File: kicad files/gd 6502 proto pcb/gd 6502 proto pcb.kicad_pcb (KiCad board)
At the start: 4 copper layers, 86.4 x 48.3 mm, 37 parts, among them J1 POWER, J10 NOR-Extra, J11 ADDR_BUS, J12 ROMEN, J2 ADDR_BUS, J3 Main Data, J4 Bus Signals, J5 Address, J6 Data, J7 ROMDIR_SEL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

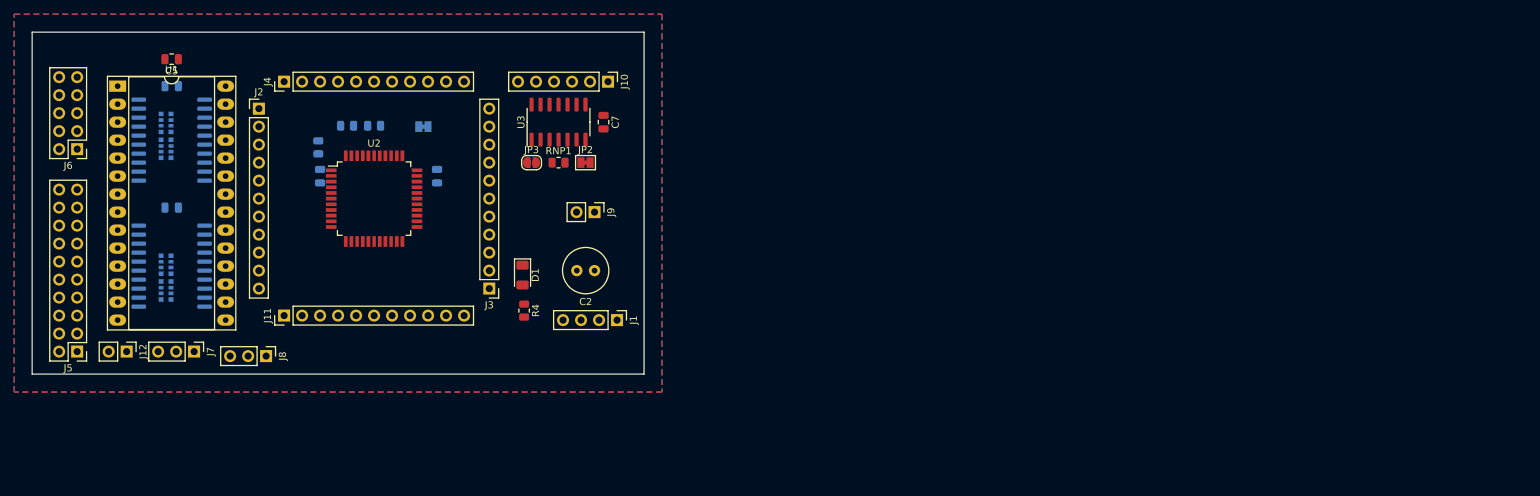
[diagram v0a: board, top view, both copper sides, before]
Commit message: can't put buffers under the eeprom. not enough room for all those address lines
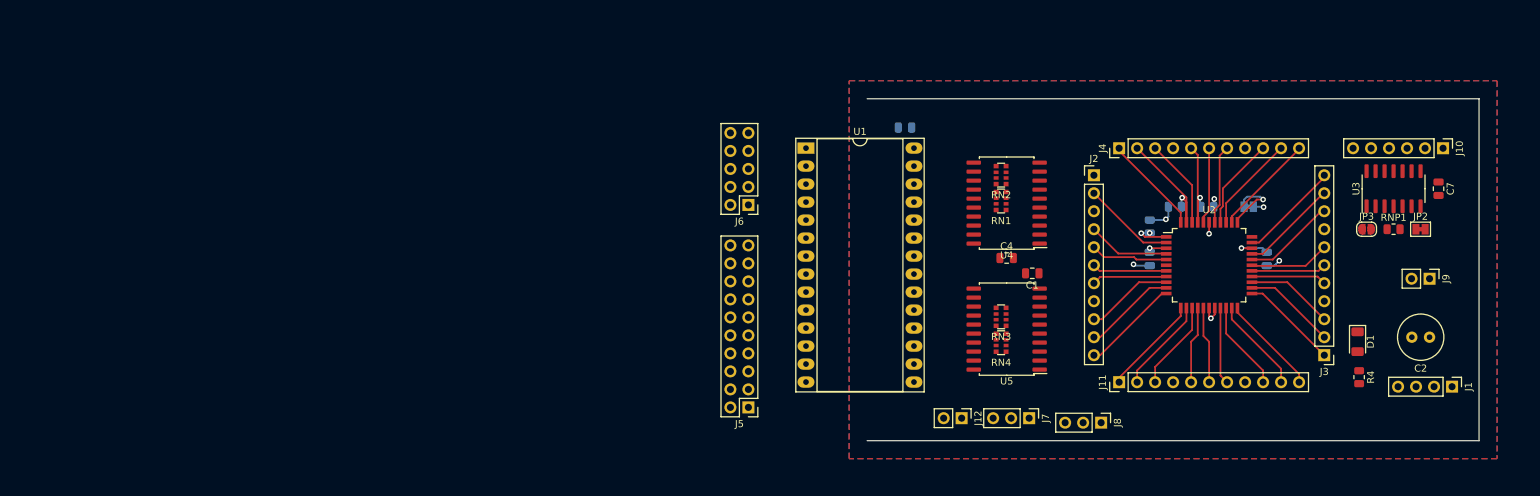
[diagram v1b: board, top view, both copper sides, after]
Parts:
- C1, C4, RN1, RN2, RN3, RN4, U4, U5: moved to F.Cu
- C5: moved to B.Cu
- moved C1 124.3 mm to (156.4, 89.9), turned to 180 degrees
- moved RN4 121.9 mm to (152.0, 99.7)
- moved U5 120.8 mm to (152.8, 97.8), turned to 180 degrees
- moved RN3 120.2 mm to (152.0, 96.1)
- moved RN2 119.0 mm to (152.0, 76.1)
- moved J8 118.2 mm to (166.1, 111.0)
- moved C2 118.2 mm to (212.5, 98.9)
- moved C7 118.2 mm to (213.7, 78.0)
- moved D1 118.2 mm to (202.3, 99.6)
- moved J10 118.2 mm to (214.4, 72.3)
- moved J11 118.2 mm to (168.7, 105.3)
- moved J12 118.2 mm to (146.4, 110.4)
- moved J4 118.2 mm to (168.7, 72.3)
- moved J9 118.2 mm to (212.5, 90.7)
- moved R4 118.2 mm to (202.5, 104.6)
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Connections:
- U4 pad 2: /A7 -> /A8
- U4 pad 3: /A6 -> /A9
- U4 pad 4: /A5 -> /A10
- U4 pad 5: /A4 -> /A11
- U4 pad 6: /A3 -> /A12
- U4 pad 7: /A2 -> /A13
- U4 pad 8: /A1 -> /A14
- U4 pad 9: /A0 -> /A15
- U5 pad 2: /A15 -> /A0
- U5 pad 3: /A14 -> /A1
- U5 pad 4: /A13 -> /A2
- U5 pad 5: /A12 -> /A3
- U5 pad 6: /A11 -> /A4
- U5 pad 7: /A10 -> /A5
- U5 pad 8: /A9 -> /A6
- U5 pad 9: /A8 -> /A7
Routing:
- net /~IRQ: track 0.00 -> 18.4 mm, vias 0 -> 1
- net /RDY: track 0.00 -> 15.8 mm, vias 0 -> 1
- net +5V: track 0.00 -> 15.1 mm, vias 0 -> 5
- net /PH0: track 0.00 -> 14.4 mm
- net /RWB: track 0.00 -> 14.3 mm
- net /A15: track 0.00 -> 14.1 mm
- net /A7: track 0.00 -> 14.1 mm
- net /MLB: track 0.00 -> 14.1 mm
- net /A6: track 0.00 -> 13.8 mm
- net /D7: track 0.00 -> 13.8 mm
- net /D0: track 0.00 -> 13.8 mm
- net /SOB: track 0.00 -> 13.7 mm
- net /A8: track 0.00 -> 13.3 mm
- net /A14: track 0.00 -> 13.3 mm
- net /A5: track 0.00 -> 13.1 mm
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
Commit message: rev1 pcb complete - whew!
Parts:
- added H1: MountingHole, MountingHole:MountingHole_2.7mm_M2.5, F.Cu at (136.1, 64.9)
- added H3: MountingHole, MountingHole:MountingHole_2.7mm_M2.5, F.Cu at (136.1, 111.8)
- added H4: MountingHole, MountingHole:MountingHole_2.7mm_M2.5, F.Cu at (220.9, 111.7)
- added He: MountingHole, MountingHole:MountingHole_2.7mm_M2.5, F.Cu at (220.9, 64.9)
- added REF**: OSHW-Symbol_6.7x6mm_SilkScreen, Symbol:OSHW-Symbol_6.7x6mm_SilkScreen, F.Cu at (220.5, 96.6)
- added REF**: KiCad-Logo_5mm_SilkScreen, Symbol:KiCad-Logo_5mm_SilkScreen, B.Cu at (192.5, 90.2)
- added svg2mod: G***, My Libraries:BE5v2, F.Cu at (183.1, 108.2)
- C1, C4: moved to B.Cu
- J1: footprint Connector_PinHeader_2.54mm:PinHeader_1x04_P2.54mm_Vertical -> Connector_PinHeader_2.54mm:PinHeader_2x02_P2.54mm_Vertical
- J10: footprint Connector_PinHeader_2.54mm:PinHeader_1x06_P2.54mm_Vertical -> Connector_PinHeader_2.54mm:PinHeader_1x07_P2.54mm_Vertical
- RN1, RN2, RN3, RN4: value R_Pack04 -> 0
- moved J5 76.8 mm to (193.1, 110.9), turned to 90 degrees
- moved J1 70.8 mm to (145.0, 110.4), turned to 90 degrees
- moved C2 61.0 mm to (152.3, 108.8), turned to 0 degrees
- moved J6 56.1 mm to (163.4, 110.9), turned to 90 degrees
- moved D1 44.9 mm to (158.7, 110.0), turned to 90 degrees
- moved J7 44.7 mm to (171.3, 68.3)
- moved J12 44.1 mm to (143.8, 66.3), turned to 90 degrees
- moved R4 44.0 mm to (158.6, 105.9), turned to 0 degrees
- moved J8 42.9 mm to (162.0, 68.3)
- moved U1 41.7 mm to (152.7, 103.0), turned to 180 degrees
- moved C5 39.5 mm to (153.3, 105.9), turned to 0 degrees
- moved J9 21.1 mm to (212.3, 69.6)
- moved JP3 17.0 mm to (216.7, 72.9)
- moved J10 16.9 mm to (213.4, 89.2), turned to 0 degrees
- moved RN1 13.4 mm to (164.1, 74.0), turned to 0 degrees
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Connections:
- J1 pad 2: +5V -> GND
- J1 pad 3: GND -> +5V
- J10 pad 1: /3A -> /PH1
- J10 pad 2: /3B -> /4Y
- J10 pad 3: /3Y -> /4B
- J10 pad 5: /4B -> /3Y
- J10 pad 6: /4Y -> /3B
- RN1 pad 1: /A0 -> /BA0
- RN1 pad 2: /A1 -> /BA1
- RN1 pad 3: /A2 -> /BA2
- RN1 pad 4: /A3 -> /BA3
- RN1 pad 5: /BA3 -> /A3
- RN1 pad 6: /BA2 -> /A2
- RN1 pad 7: /BA1 -> /A1
- RN1 pad 8: /BA0 -> /A0
- RN2 pad 1: /A4 -> /BA4
- RN2 pad 2: /A5 -> /BA5
- RN2 pad 3: /A6 -> /BA6
- RN2 pad 4: /A7 -> /BA7
- RN2 pad 5: /BA7 -> /A7
- RN2 pad 6: /BA6 -> /A6
- RN2 pad 7: /BA5 -> /A5
- RN2 pad 8: /BA4 -> /A4
- RN3 pad 1: /A8 -> /BA8
- RN3 pad 2: /A9 -> /BA9
- RN3 pad 3: /A10 -> /BA10
- RN3 pad 4: /A11 -> /BA11
- RN3 pad 5: /BA11 -> /A11
- RN3 pad 6: /BA10 -> /A10
- RN3 pad 7: /BA9 -> /A9
- RN3 pad 8: /BA8 -> /A8
- RN4 pad 1: /A12 -> /BA12
- RN4 pad 2: /A13 -> /BA13
- RN4 pad 3: /A14 -> Net-(RN4-Pad3)
- RN4 pad 4: /A15 -> Net-(RN4-Pad4)
- RN4 pad 5: /BA15 -> Net-(RN4-Pad5)
- RN4 pad 6: /BA14 -> Net-(RN4-Pad6)
- RN4 pad 7: /BA13 -> /A13
- RN4 pad 8: /BA12 -> /A12
- U4 pad 2: /A8 -> /A7
- U4 pad 3: /A9 -> /A6
- U4 pad 4: /A10 -> /A5
- U4 pad 5: /A11 -> /A4
- U4 pad 6: /A12 -> /A3
- U4 pad 7: /A13 -> /A2
- U4 pad 8: /A14 -> /A1
- U4 pad 9: /A15 -> /A0
- U5 pad 17: /BA14 -> Net-(U5-Pad17)
- U5 pad 18: /BA15 -> Net-(U5-Pad18)
- U5 pad 2: /A0 -> Net-(U5-Pad2)
- U5 pad 3: /A1 -> Net-(U5-Pad3)
- U5 pad 4: /A2 -> /A13
- U5 pad 5: /A3 -> /A12
- U5 pad 6: /A4 -> /A11
- U5 pad 7: /A5 -> /A10
- U5 pad 8: /A6 -> /A9
- U5 pad 9: /A7 -> /A8
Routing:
- net /D3: track 10.5 -> 143.3 mm, vias 0 -> 2
- net /D0: track 13.8 -> 141.0 mm
- net /D4: track 10.6 -> 130.2 mm, vias 0 -> 1
- net /D6: track 13.1 -> 130.8 mm, vias 0 -> 2
- net /D5: track 12.4 -> 127.5 mm, vias 0 -> 1
- net /D2: track 11.3 -> 121.6 mm, vias 0 -> 1
- net /D1: track 13.0 -> 121.8 mm
- net /D7: track 13.8 -> 115.5 mm, vias 0 -> 2
- net /A5: track 13.1 -> 79.2 mm
- net /A6: track 13.8 -> 79.8 mm
- net /A3: track 10.6 -> 76.2 mm
- net /A4: track 12.4 -> 76.0 mm
- net /A0: track 11.6 -> 72.5 mm, vias 0 -> 1
- net /A12: track 10.8 -> 71.0 mm
- net /A2: track 10.5 -> 70.2 mm
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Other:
- board size 86.4 x 48.3 mm -> 90.4 x 52.2 mm
- board text added: "3A"
- board text added: "3B"
- board text added: "3Y"
- board text added: "4A"
- board text added: "4B"
- board text added: "4Y"
- board text added: "5V"
- board text added: "A0"
- board text added: "A1"
- board text added: "A10"
- board text added: "A11"
- board text added: "A12"
- board text added: "A13"
- board text added: "A14"
- board text added: "A15"
- board text added: "A2"
- board text added: "A3"
- board text added: "A4"
- board text added: "A5"
- board text added: "A6"
- board text added: "A7"
- board text added: "A8"
- board text added: "A9"
- board text added: "Address"
- board text added: "D0"
- board text added: "D1"
- board text added: "D2"
- board text added: "D3"
- board text added: "D4"
- board text added: "D5"
- board text added: "D6"
- board text added: "D7"
- board text added: "DIR"
- board text added: "DMA"
- board text added: "Data"
- board text added: "GD 65c02 @baldengineer rev1"
- board text added: "GND"
- board text added: "MLB"
- board text added: "PH0"
- board text added: "PH0_ALT"
- board text added: "PH1"
- board text added: "PHI10"
- board text added: "PHI2O"
- board text added: "RDY"
- board text added: "RWB"
- board text added: "SOB"
- board text added: "Thanks Chat! You Look Great Today!"
- board text added: "VPB"
- board text added: "~EN"
- board text added: "~G"
- board text added: "~IRQ"
- board text added: "~NMI"
- board text added: "~RES"
- board text added: "~ROMEN"
- board text added: "~SYNC"
